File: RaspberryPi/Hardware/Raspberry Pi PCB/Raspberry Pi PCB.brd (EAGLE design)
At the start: 70 x 80 mm, 1 part

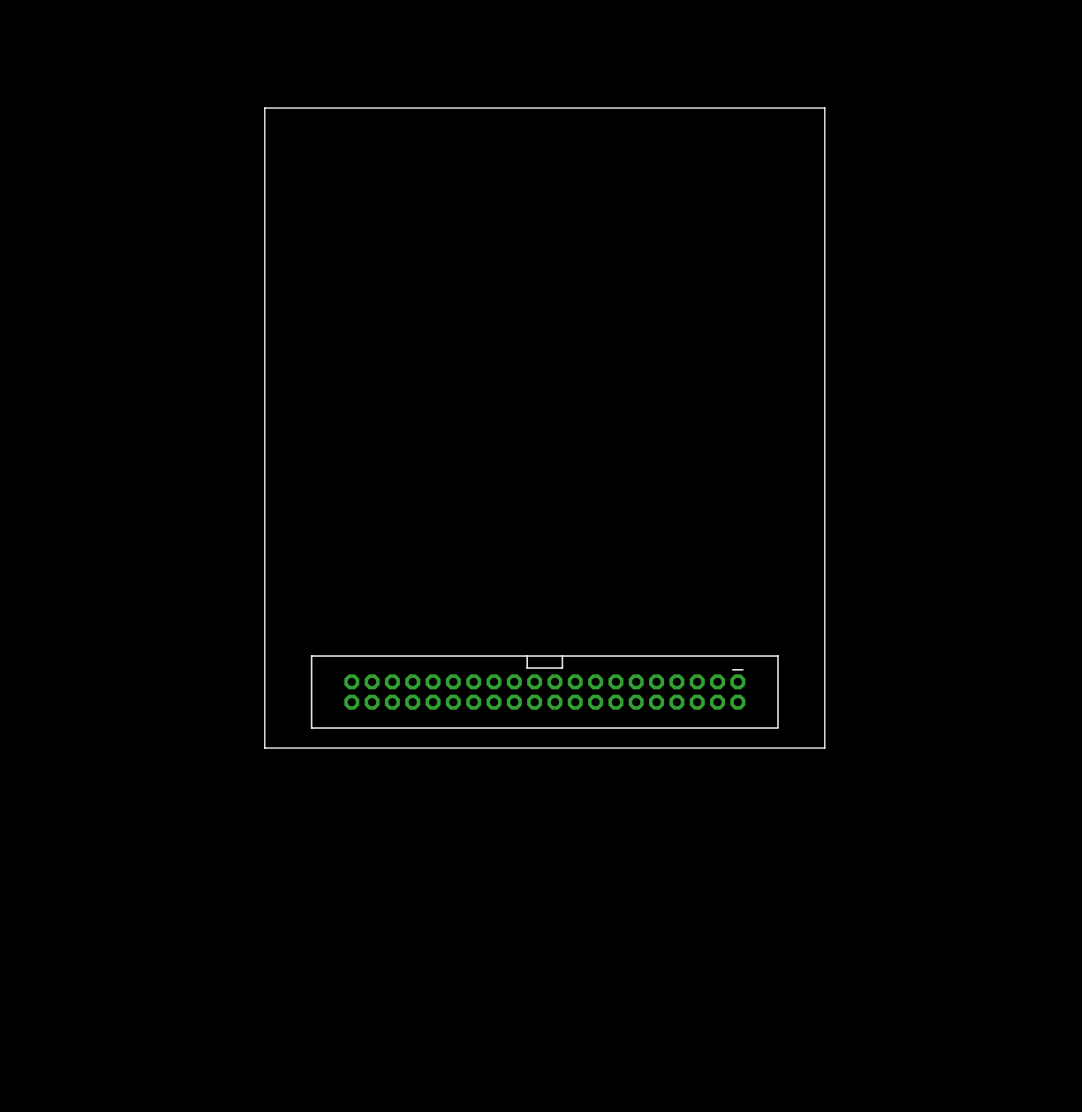
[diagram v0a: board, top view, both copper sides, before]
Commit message: Added some necessary components for powering the Raspberry.
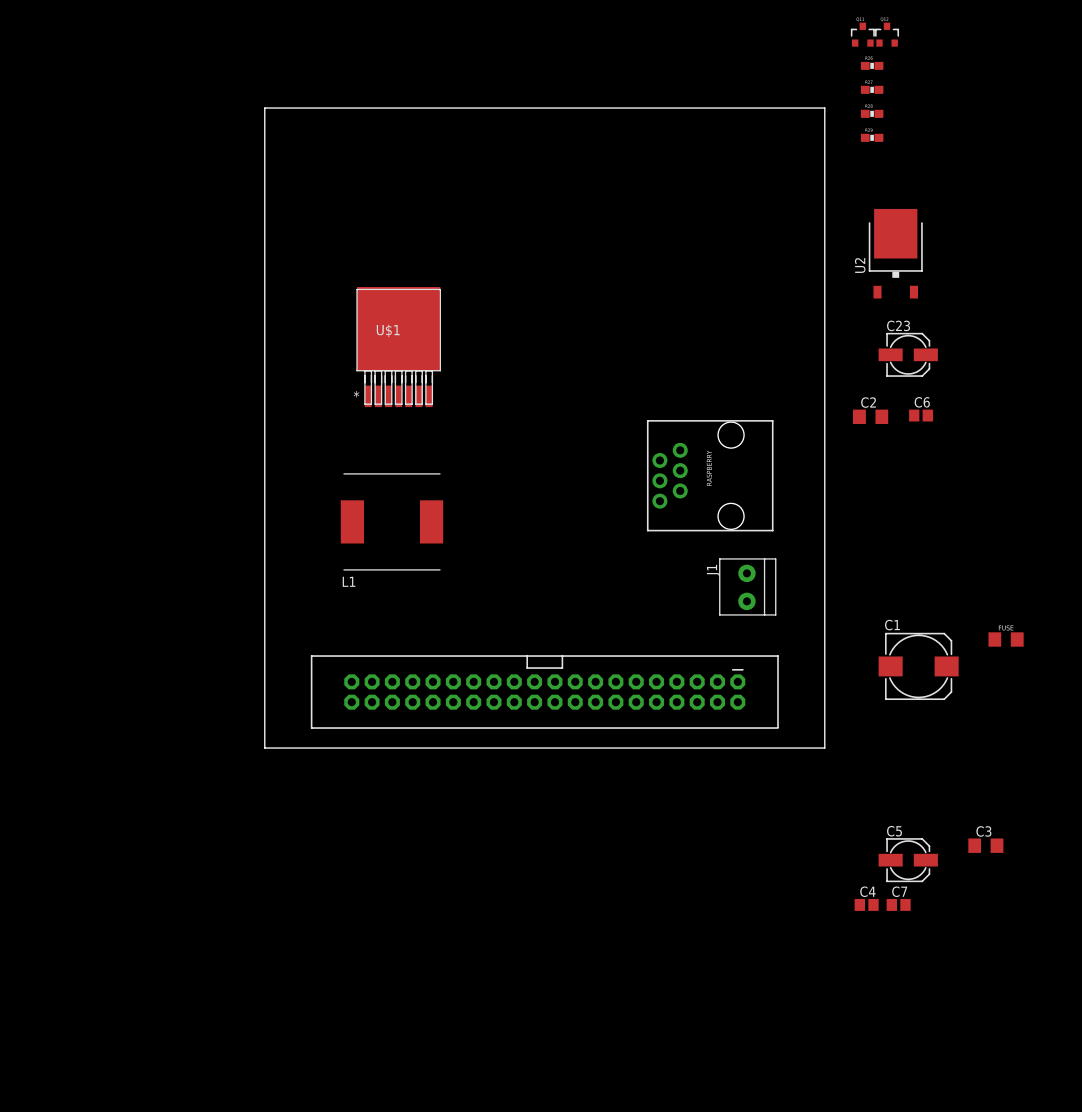
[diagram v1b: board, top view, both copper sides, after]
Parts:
- added C1: 220uF, adafruit:175TMP-0810
- added C2: 220pF, adafruit:C1206
- added C23: 22uF, adafruit:153CLV-0505
- added C3: (no value), adafruit:C1206
- added C4, C7: (no value), adafruit:C0805
- added C5: (no value), adafruit:153CLV-0505
- added C6: 100nF, adafruit:C0805
- added FUSE: 6V/0.5A, SparkFun-Fuses:1206
- added J1: 1X2-3.5MM, adafruit:1X2-3.5MM
- added L1: (no value), WE-PD:WE-PD_1260/1245/1280/1210
- added Q11, Q12: BSS138, SparkFun:SOT23-3
- added R26, R27, R28, R29: 10K, SparkFun:0603-RES
- added RASPBERRY: RJ11, SparkFun-Connectors:RJ11-6
- added U$1: LM2670SX-5.0/NOPB, LM2670:TS7B
- added U2: 7812DT, adafruit:TO252
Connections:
- new net +12V: C23.+, C6.1, Q11.1, R26.1, R29.1, U2.2
- new net +24V: C1.+, C2.1, C3.1, FUSE.2, U$1.2, U2.1
- new net DATA_RASPI: RASPBERRY.1
- new net ON/OFF: U$1.7
- new net RES_RASPI: RASPBERRY.4
- new net RX_ATXMEGA: Q11.3, R27.2
- new net RX_RASPI: Q12.3, R29.2, RASPBERRY.5
- new net TX_ATXMEGA: Q12.2, R28.2
- new net TX_RASPI: Q11.2, R26.2, RASPBERRY.3
- new net VCC: RASPBERRY.6
- new net VIN: FUSE.1, J1.2
- net 3.3V: now also Q12.1, R27.1, R28.1
- net 5V: now also C4.1, C5.+, C7.1
- net GND: now also C1.-, C2.2, C23.-, C3.2, C4.2, C5.-, C6.2, C7.2, J1.1, RASPBERRY.2, U$1.4, U2.3

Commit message: Power component changes.
The planned buck converter will not be used on the PCB. It was decided that an AC/DC converter will be used that was available from the first Bidon dispenser project. This converter already outputs the desired 5V with a sufficient current.
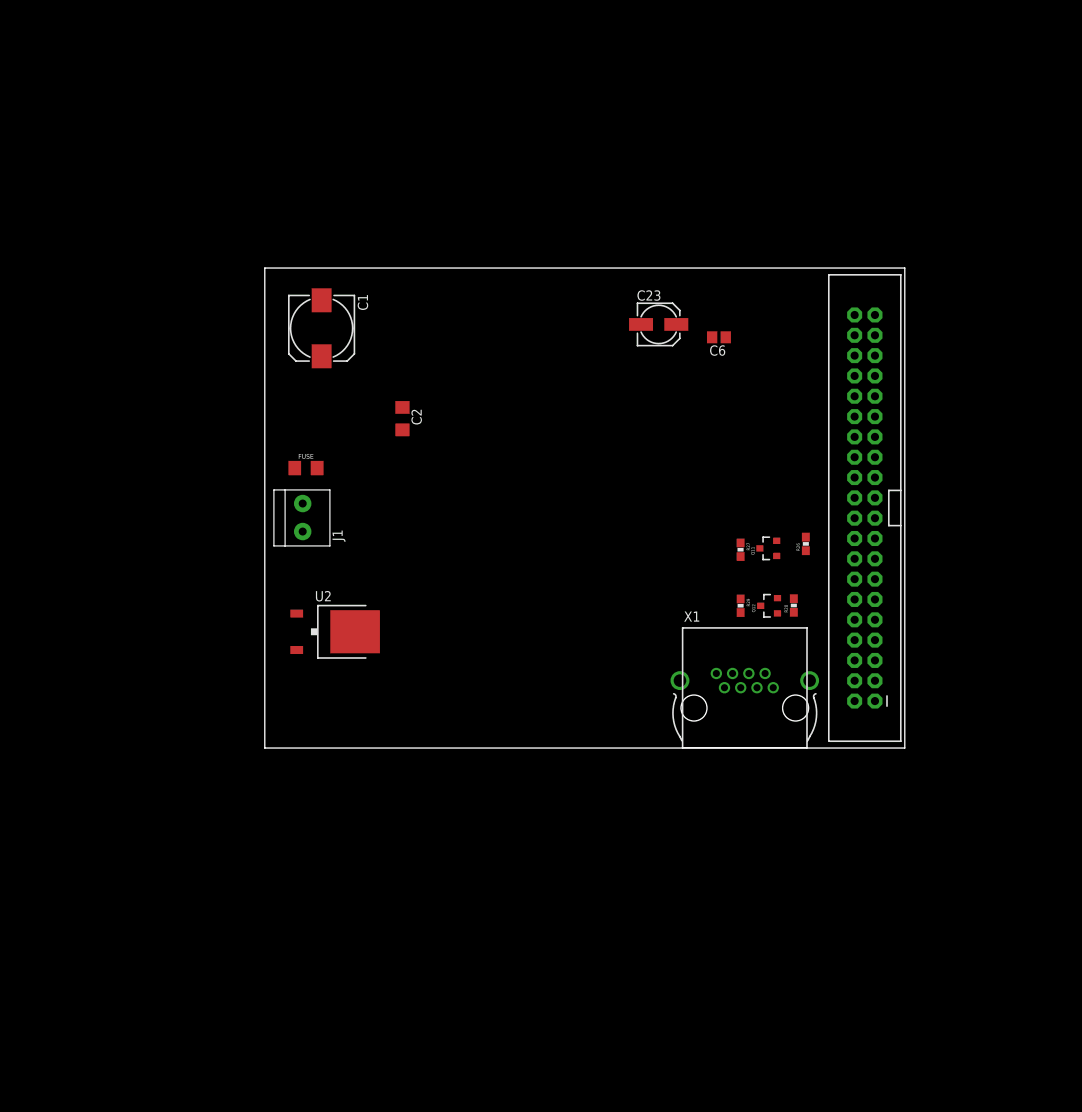
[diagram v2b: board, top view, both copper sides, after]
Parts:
- removed C3: (no value), adafruit:C1206
- removed C4, C7: (no value), adafruit:C0805
- removed C5: (no value), adafruit:153CLV-0505
- removed L1: (no value), WE-PD:WE-PD_1260/1245/1280/1210
- removed RASPBERRY: RJ11, SparkFun-Connectors:RJ11-6
- removed U$1: LM2670SX-5.0/NOPB, LM2670:TS7B
- added X1: 0446200002, con-molex:0446200002
- moved FUSE 90.1 mm to (5.15, 35.0)
- moved C1 85.8 mm to (7.10, 52.5), turned to 270 degrees
- moved U2 84.5 mm to (8.79, 14.5), turned to 270 degrees
- moved Q12 72.8 mm to (63.1, 17.8), turned to 90 degrees
- moved Q11 65.2 mm to (63.0, 25.0), turned to 90 degrees
- moved R28 62.2 mm to (66.1, 17.8), turned to 90 degrees
- moved R29 60.8 mm to (59.5, 17.8), turned to 270 degrees
- moved R26 60.3 mm to (67.6, 25.5), turned to 90 degrees
- moved R27 59.8 mm to (59.5, 24.8), turned to 270 degrees
- moved C2 58.5 mm to (17.2, 41.2), turned to 270 degrees
- moved J1 56.2 mm to (4.74, 28.9), turned to 270 degrees
- moved JP2 46.1 mm to (75.0, 30.0), turned to 180 degrees
- moved C23 31.4 mm to (49.2, 52.9)
- moved C6 27.1 mm to (56.8, 51.3), turned to 180 degrees
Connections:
- removed net DATA_RASPI: RASPBERRY.1
- removed net ON/OFF: U$1.7
- removed net RES_RASPI: RASPBERRY.4
- removed net RXI: JP2.10
- removed net TXO: JP2.8
- removed net VCC: RASPBERRY.6
- net +12V: now also X1.2
- net +24V: no longer C3.1, U$1.2
- net 5V: no longer C4.1, C5.+, C7.1
- net GND: now also X1.1, X1.3, X1.5, X1.7, X1.S@1, X1.S@2; no longer C3.2, C4.2, C5.-, C7.2, RASPBERRY.2, U$1.4
- net RX_ATXMEGA: now also Q12.3, R29.2, X1.4; no longer Q11.3, R27.2
- net RX_RASPI: now also JP2.10, Q11.3, R27.2; no longer Q12.3, R29.2, RASPBERRY.5
- net TX_ATXMEGA: now also Q11.2, R26.2, X1.6; no longer Q12.2, R28.2
- net TX_RASPI: now also JP2.8, Q12.2, R28.2; no longer Q11.2, R26.2, RASPBERRY.3
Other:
- board size 70 x 80 mm -> 80 x 60 mm

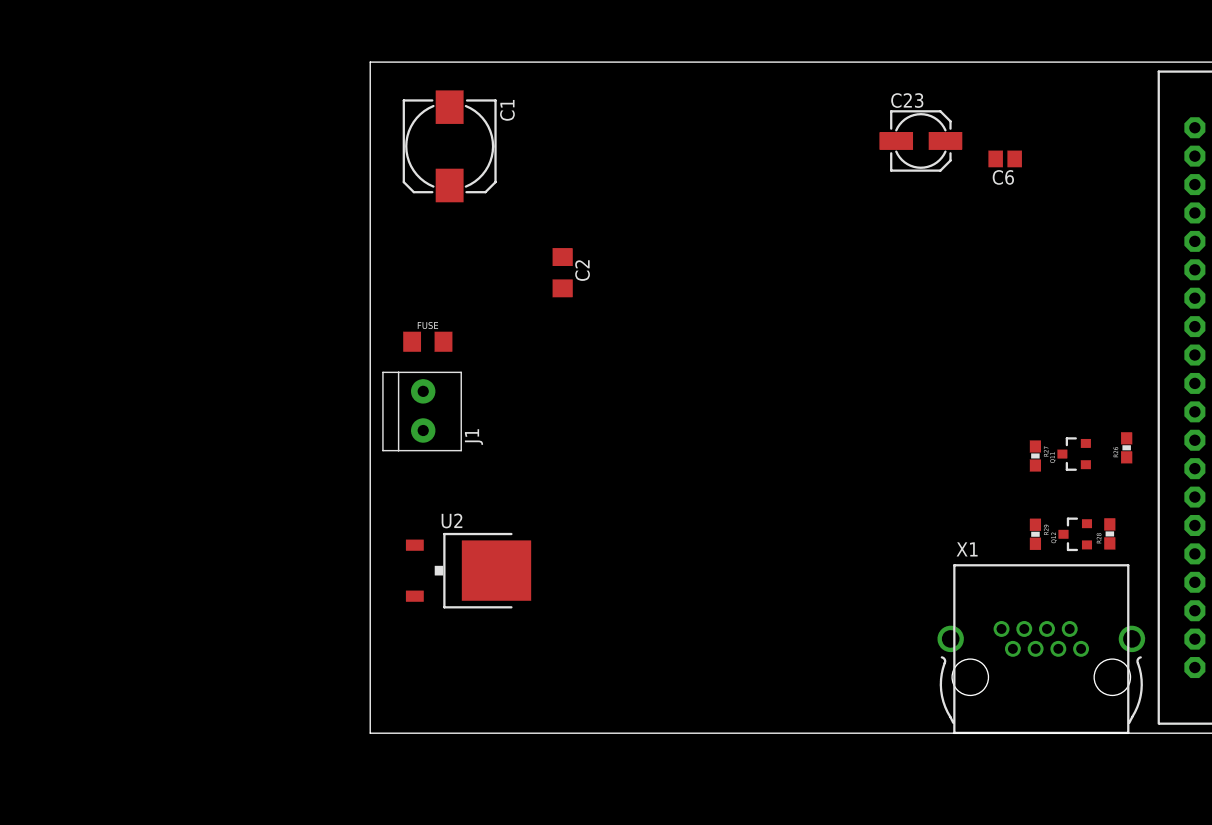
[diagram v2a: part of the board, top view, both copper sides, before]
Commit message: Added a step up converter.
This step up is required for the 12 volt data communication between the Raspberry and the microcontroller. It ofcourse also works with the lower 5 volt, but for reliability we use 12 volt.
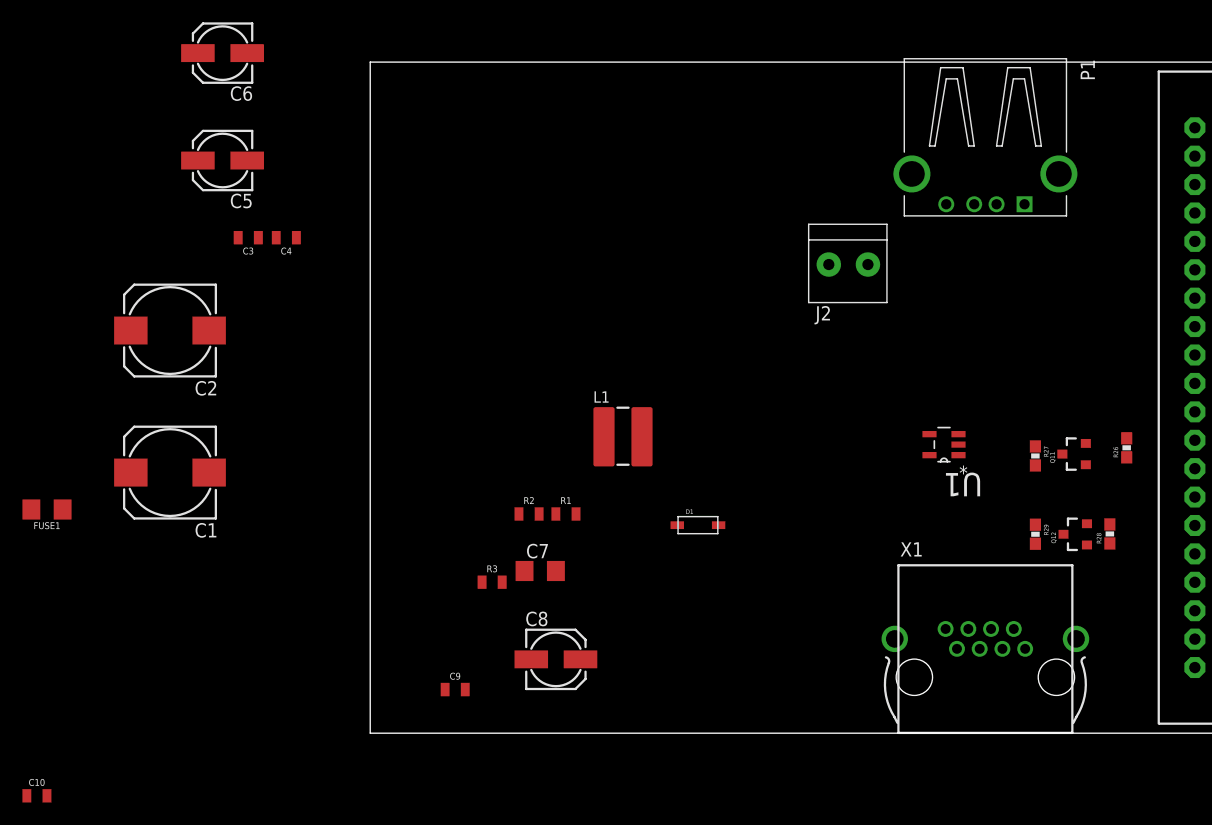
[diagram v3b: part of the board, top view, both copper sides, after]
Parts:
- removed C23: 22uF, adafruit:153CLV-0505
- removed FUSE: 6V/0.5A, SparkFun-Fuses:1206
- removed J1: 1X2-3.5MM, adafruit:1X2-3.5MM
- removed U2: 7812DT, adafruit:TO252
- added C10, C3, C4, C9: 100nF, SparkFun-Capacitors:0805
- added C5, C8: 10uF, adafruit:153CLV-0505
- added C7: (no value), adafruit:C1206
- added D1: (no value), adafruit:SOD-123
- added FUSE1: 6V/0.5A, SparkFun-Fuses:1206
- added J2: 1X2-3.5MM, adafruit:1X2-3.5MM
- added L1: CDRH4D18, inductor-sumida:CDRH4D18
- added P1: 87520-0010BLF, 87520-0010BLF:FCI_87520-0010BLF
- added R1, R2, R3: (no value), SparkFun-Resistors:0805
- added U1: TPS61040QDBVRQ1, Texas Instruments_By_element14_Batch_1:SOT95P280X145-5N
- C1: value 220uF -> 100uF
- C2: value 220pF -> 100uF; device adafruit:C1206 -> adafruit:175TMP-0810
- C6: value 100nF -> 10uF; device adafruit:C0805 -> adafruit:153CLV-0505
- moved C6 70.6 mm to (-13.2, 60.8)
- moved C1 38.4 mm to (-17.9, 23.3), turned to 180 degrees
- moved C2 35.5 mm to (-17.9, 36.0), turned to 180 degrees
- moved X1 5.00 mm to (55.0, 5.00)
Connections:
- removed net +24V: C1.+, C2.1, FUSE.2, U2.1
- removed net VIN: FUSE.1, J1.2
- new net +5V: C1.+, C2.+, C3.1, C4.1, C5.+, C6.+, FUSE1.2, L1.1, U1.4, U1.5
- new net FEEDBACK: C7.2, R1.1, R2.2, U1.3
- new net N$1: D1.A, L1.2, U1.1
- new net N$2: R2.1, R3.2
- new net VIN1: FUSE1.1, J2.2
- net +12V: now also C7.1, C8.+, C9.1, D1.C, R1.2; no longer C23.+, C6.1, U2.2
- net 5V: now also C10.1, P1.1
- net GND: now also C10.2, C2.-, C3.2, C4.2, C5.-, C6.-, C8.-, C9.2, J2.1, P1.4, R3.1, U1.2; no longer C2.2, C23.-, C6.2, J1.1, U2.3
